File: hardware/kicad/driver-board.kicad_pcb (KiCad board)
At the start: 4 copper layers, 42.2 x 36.8 mm, 57 parts, among them J1 Conn_01x13_Male, U1 TXS0108E, U2 ME6210, U3 ME6210, U4 TLV61046ADB, U5 NC7SZ125, U6 FT813, U7 ER-TFT040-2, X1 YSX321SL

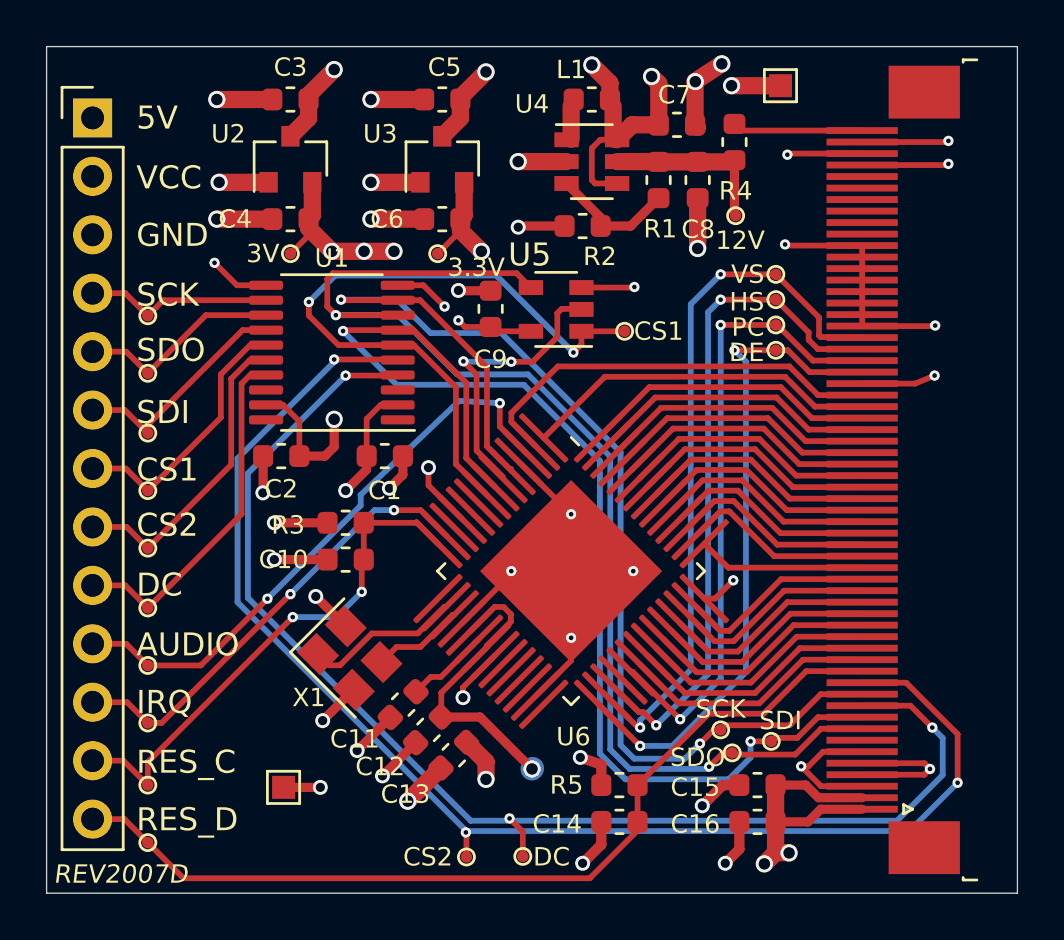
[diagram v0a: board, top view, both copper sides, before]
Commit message: Change min drill size to 0.3
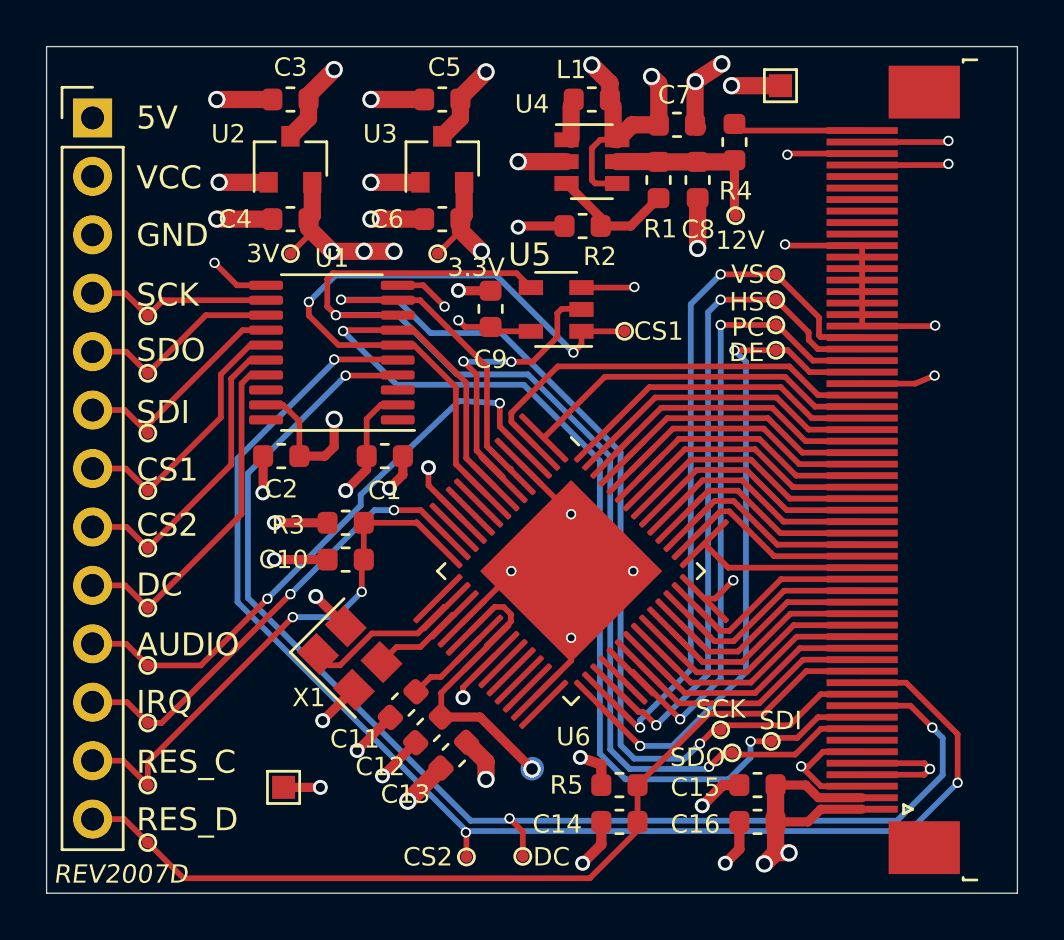
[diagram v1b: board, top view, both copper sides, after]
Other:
- net class Default: via_drill 0.2 -> 0.3
- rule via_min_drill: 0.2 -> 0.3

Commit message: Rework display reset circuit and improve 3v power supply
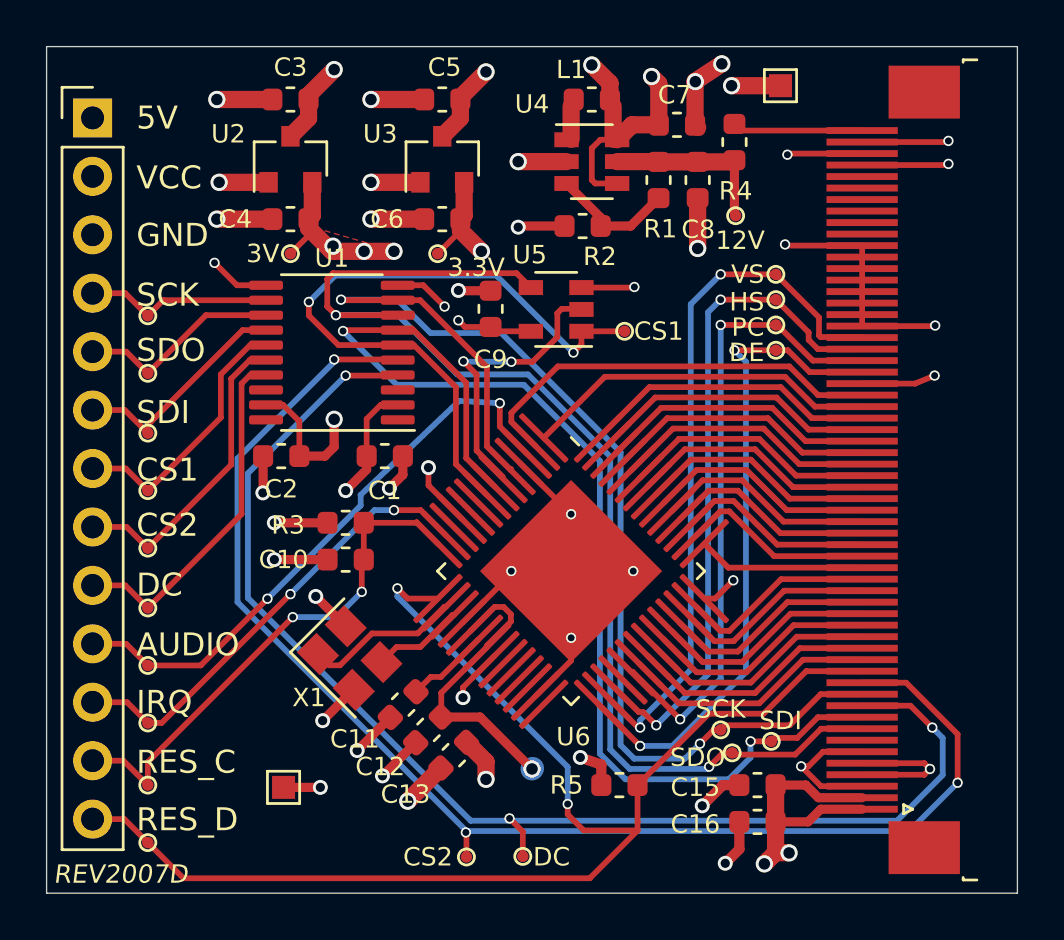
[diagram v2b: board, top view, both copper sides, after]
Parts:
- removed C14: 1µF, Capacitor_SMD:C_0603_1608Metric
- removed REF**: OSHW-Logo_5.7x6mm_SilkScreen, Symbol:OSHW-Logo_5.7x6mm_SilkScreen
- U2: value ME6210 -> ME6210A30M3G
- U3: value ME6210 -> ME6210A33M3G
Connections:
- R5 pad 2: GND -> +3V0
- U6 pad 15: Net-(U6-Pad15) -> DISPRES
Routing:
- net DISPRES: track 39.4 -> 57.6 mm, vias 0 -> 2
- net GND: track 110.8 -> 109.0 mm, vias 39 -> 38
- added copper zone on F.Cu, net +3V0
